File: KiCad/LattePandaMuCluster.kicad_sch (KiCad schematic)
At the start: 0 parts

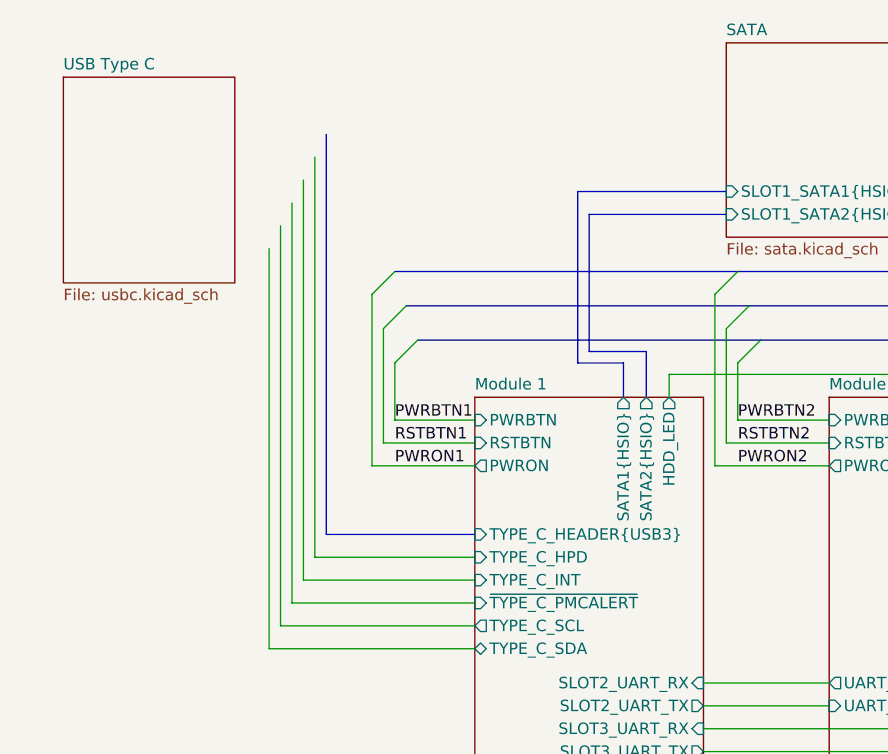
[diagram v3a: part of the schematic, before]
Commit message: Connect TPS65987D I2C and Interrupts
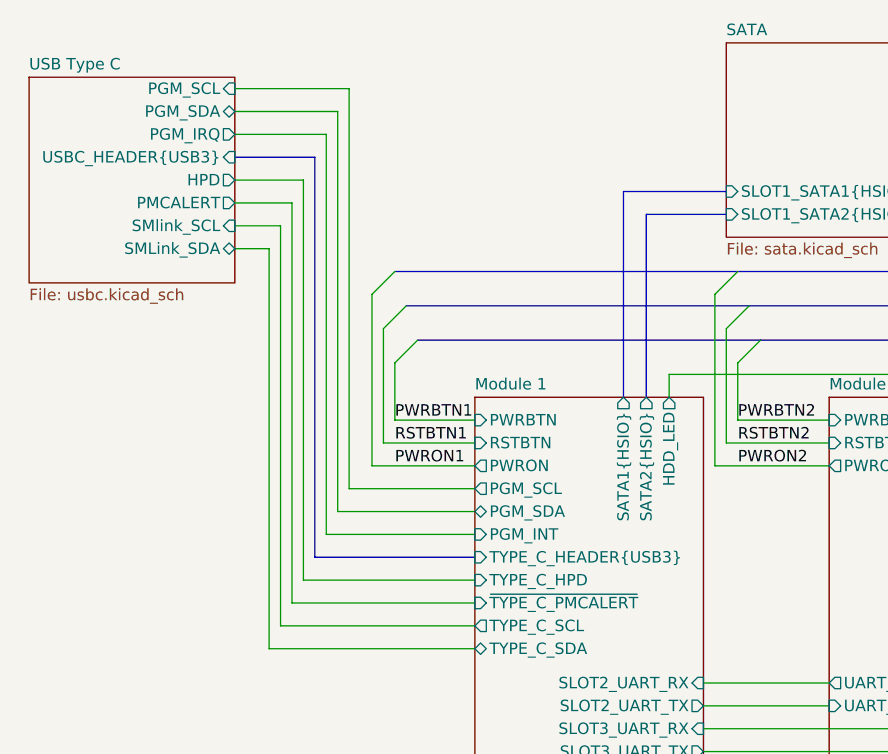
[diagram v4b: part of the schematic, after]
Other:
- sheet Module 1 ports: added PGM_INT, PGM_SCL, PGM_SDA; removed TYPE_C_INT
- sheet USB Type C ports: added HPD, PGM_IRQ, PGM_SCL, PGM_SDA, PMCALERT, SMLink_SDA, SMlink_SCL, USBC_HEADER{USB3}; removed none
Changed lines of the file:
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@@
 	(wire
 		(pts
-			(xy 81.28 158.75) (xy 81.28 168.91)
-		)
-		(stroke
-			(width 0)
-			(type default)
-		)
-	)
-	(bus
-		(pts
-			(xy 74.93 50.8) (xy 80.01 50.8)
+			(xy 46.99 69.85) (xy 63.5 69.85)
 		)
 		(stroke
@@
 		)
 	)
-	(bus
+	(wire
 		(pts
-			(xy 76.2 34.29) (xy 76.2 49.53)
+			(xy 81.28 158.75) (xy 81.28 168.91)
 		)
 		(stroke
@@
 	(wire
 		(pts
+			(xy 46.99 25.4) (xy 46.99 69.85)
+		)
+		(stroke
+			(width 0)
+			(type default)
+		)
+	)
+	(wire
+		(pts
 			(xy 88.9 101.6) (xy 196.85 101.6)
 		)
@@
 	(wire
 		(pts
-			(xy 45.72 72.39) (xy 45.72 27.94)
+			(xy 49.53 64.77) (xy 63.5 64.77)
+		)
+		(stroke
+			(width 0)
+			(type default)
+		)
+	)
+	(wire
+		(pts
+			(xy 44.45 74.93) (xy 44.45 30.48)
 		)
 		(stroke
@@
 		)
 	)
+	(wire
+		(pts
+			(xy 36.83 22.86) (xy 48.26 22.86)
+		)
+		(stroke
+			(width 0)
+			(type default)
+		)
+	)
 	(bus
 		(pts
@@
 	(wire
 		(pts
+			(xy 36.83 35.56) (xy 41.91 35.56)
+		)
+		(stroke
+			(width 0)
+			(type default)
+		)
+	)
+	(wire
+		(pts
 			(xy 43.18 77.47) (xy 43.18 33.02)
 		)
@@
 		)
 	)
+	(wire
+		(pts
+			(xy 36.83 38.1) (xy 40.64 38.1)
+		)
+		(stroke
+			(width 0)
+			(type default)
+		)
+	)
 	(bus
 		(pts
@@
 	(bus
 		(pts
-			(xy 76.2 49.53) (xy 82.55 49.53)
-		)
-		(stroke
-			(width 0)
-			(type default)
-		)
-	)
-	(bus
-		(pts
 			(xy 196.85 138.43) (xy 189.23 138.43)
 		)
@@
 	(bus
 		(pts
-			(xy 74.93 31.75) (xy 91.44 31.75)
+			(xy 80.01 31.75) (xy 91.44 31.75)
 		)
 		(stroke
@@
 	(bus
 		(pts
-			(xy 46.99 69.85) (xy 63.5 69.85)
+			(xy 45.72 72.39) (xy 63.5 72.39)
 		)
 		(stroke
@@
 	(bus
 		(pts
-			(xy 80.01 50.8) (xy 80.01 54.61)
-		)
-		(stroke
-			(width 0)
-			(type default)
-		)
-	)
-	(bus
-		(pts
 			(xy 218.44 153.67) (xy 220.98 153.67)
 		)
@@
 	(wire
 		(pts
+			(xy 36.83 20.32) (xy 49.53 20.32)
+		)
+		(stroke
+			(width 0)
+			(type default)
+		)
+	)
+	(wire
+		(pts
 			(xy 53.34 59.69) (xy 63.5 59.69)
 		)
@@
 	(wire
 		(pts
+			(xy 36.83 25.4) (xy 46.99 25.4)
+		)
+		(stroke
+			(width 0)
+			(type default)
+		)
+	)
+	(wire
+		(pts
 			(xy 90.17 162.56) (xy 90.17 168.91)
 		)
@@
 	(wire
 		(pts
+			(xy 49.53 20.32) (xy 49.53 64.77)
+		)
+		(stroke
+			(width 0)
+			(type default)
+		)
+	)
+	(wire
+		(pts
 			(xy 90.17 43.18) (xy 90.17 62.23)
 		)
@@
 	(wire
 		(pts
-			(xy 124.46 57.15) (xy 134.62 57.15)
+			(xy 36.83 33.02) (xy 43.18 33.02)
 		)
 		(stroke
@@
 		)
 	)
-	(bus
+	(wire
 		(pts
-			(xy 46.99 25.4) (xy 46.99 69.85)
+			(xy 124.46 57.15) (xy 134.62 57.15)
 		)
 		(stroke
@@
 	(bus
 		(pts
+			(xy 36.83 27.94) (xy 45.72 27.94)
+		)
+		(stroke
+			(width 0)
+			(type default)
+		)
+	)
+	(wire
+		(pts
+			(xy 48.26 22.86) (xy 48.26 67.31)
+		)
+		(stroke
+			(width 0)
+			(type default)
+		)
+	)
+	(bus
+		(pts
+			(xy 45.72 27.94) (xy 45.72 72.39)
+		)
+		(stroke
+			(width 0)
+			(type default)
+		)
+	)
+	(bus
+		(pts
 			(xy 128.27 154.94) (xy 76.2 154.94)
 		)
@@
 	(wire
 		(pts
-			(xy 44.45 74.93) (xy 44.45 30.48)
-		)
-		(stroke
-			(width 0)
-			(type default)
-		)
-	)
-	(wire
-		(pts
 			(xy 90.17 62.23) (xy 102.87 62.23)
 		)
@@
 	(bus
 		(pts
-			(xy 76.2 34.29) (xy 91.44 34.29)
+			(xy 82.55 34.29) (xy 91.44 34.29)
 		)
 		(stroke
@@
 	(bus
 		(pts
-			(xy 74.93 31.75) (xy 74.93 50.8)
+			(xy 80.01 31.75) (xy 80.01 54.61)
 		)
 		(stroke
@@
 	(wire
 		(pts
+			(xy 48.26 67.31) (xy 63.5 67.31)
+		)
+		(stroke
+			(width 0)
+			(type default)
+		)
+	)
+	(wire
+		(pts
 			(xy 123.19 46.99) (xy 123.19 59.69)
 		)
@@
 	(wire
 		(pts
-			(xy 63.5 74.93) (xy 44.45 74.93)
+			(xy 36.83 30.48) (xy 44.45 30.48)
 		)
 		(stroke
@@
 	(bus
 		(pts
-			(xy 82.55 49.53) (xy 82.55 54.61)
+			(xy 82.55 34.29) (xy 82.55 54.61)
 		)
 		(stroke
@@
 	(wire
 		(pts
-			(xy 63.5 72.39) (xy 45.72 72.39)
+			(xy 63.5 74.93) (xy 44.45 74.93)
 		)
 		(stroke
@@
 		)
 		(pin "TYPE_C_HEADER{USB3}" input
-			(at 63.5 69.85 180)
+			(at 63.5 72.39 180)
 			(effects
 				(font
@@
 		)
 		(pin "TYPE_C_HPD" input
-			(at 63.5 72.39 180)
-			(effects
-				(font
-					(size 1.27 1.27)
-				)
-				(justify left)
-			)
-		)
-		(pin "TYPE_C_INT" input
 			(at 63.5 74.93 180)
 			(effects
@@
 			)
 		)
+		(pin "PGM_INT" input
+			(at 63.5 69.85 180)
+			(effects
+				(font
+					(size 1.27 1.27)
+				)
+				(justify left)
+			)
+		)
+		(pin "PGM_SCL" output
+			(at 63.5 64.77 180)
+			(effects
+				(font
+					(size 1.27 1.27)
+				)
+				(justify left)
+			)
+		)
+		(pin "PGM_SDA" bidirectional
+			(at 63.5 67.31 180)
+			(effects
+				(font
+					(size 1.27 1.27)
+				)
+				(justify left)
+			)
+		)
 		(instances
 			(project "LattePandaMuCluster"
@@
 	)
 	(sheet
-		(at 17.78 19.05)
-		(size 19.05 22.86)
+		(at 13.97 19.05)
+		(size 22.86 22.86)
 		(exclude_from_sim no)
 		(in_bom yes)
@@
 		)
 		(property "Sheetname" "USB Type C"
-			(at 17.78 18.3384 0)
+			(at 13.97 18.3384 0)
 			(effects
 				(font
@@
 		)
 		(property "Sheetfile" "usbc.kicad_sch"
-			(at 17.78 42.4946 0)
+			(at 13.97 42.4946 0)
 			(effects
 				(font
@@
 			)
 		)
+		(pin "HPD" output
+			(at 36.83 30.48 0)
+			(effects
+				(font
+					(size 1.27 1.27)
+				)
+				(justify right)
+			)
+		)
+		(pin "PGM_IRQ" output
+			(at 36.83 25.4 0)
+			(effects
+				(font
+					(size 1.27 1.27)
+				)
+				(justify right)
+			)
+		)
+		(pin "PGM_SCL" input
+			(at 36.83 20.32 0)
+			(effects
+				(font
+					(size 1.27 1.27)
+				)
+				(justify right)
+			)
+		)
+		(pin "PGM_SDA" bidirectional
+			(at 36.83 22.86 0)
+			(effects
+				(font
+					(size 1.27 1.27)
+				)
+				(justify right)
+			)
+		)
+		(pin "PMCALERT" output
+			(at 36.83 33.02 0)
+			(effects
+				(font
+					(size 1.27 1.27)
+				)
+				(justify right)
+			)
+		)
+		(pin "SMlink_SCL" input
+			(at 36.83 35.56 0)
+			(effects
+				(font
+					(size 1.27 1.27)
+				)
+				(justify right)
+			)
+		)
+		(pin "SMLink_SDA" bidirectional
+			(at 36.83 38.1 0)
+			(effects
+				(font
+					(size 1.27 1.27)
+				)
+				(justify right)
+			)
+		)
+		(pin "USBC_HEADER{USB3}" input
+			(at 36.83 27.94 0)
+			(effects
+				(font
+					(size 1.27 1.27)
+				)
+				(justify right)
+			)
+		)

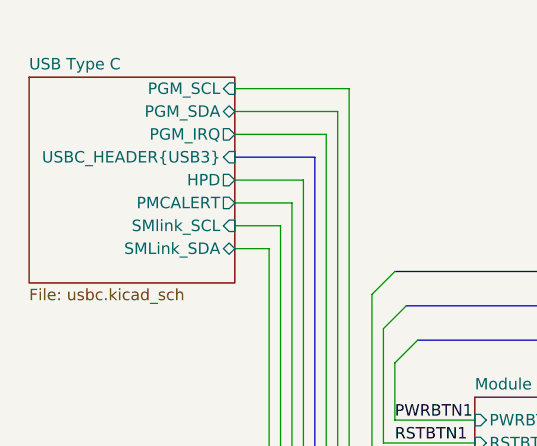
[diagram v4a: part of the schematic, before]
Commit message: Finish wiring TPS65987D
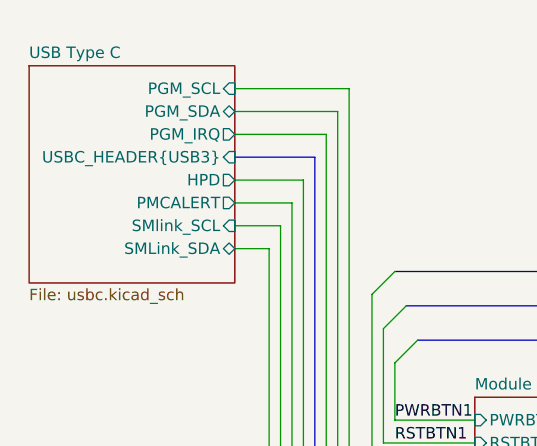
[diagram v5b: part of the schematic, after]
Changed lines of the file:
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@@
 	)
 	(sheet
-		(at 13.97 19.05)
-		(size 22.86 22.86)
+		(at 13.97 17.78)
+		(size 22.86 24.13)
 		(exclude_from_sim no)
 		(in_bom yes)
@@
 		)
 		(property "Sheetname" "USB Type C"
-			(at 13.97 18.3384 0)
+			(at 13.97 17.0684 0)
 			(effects
 				(font

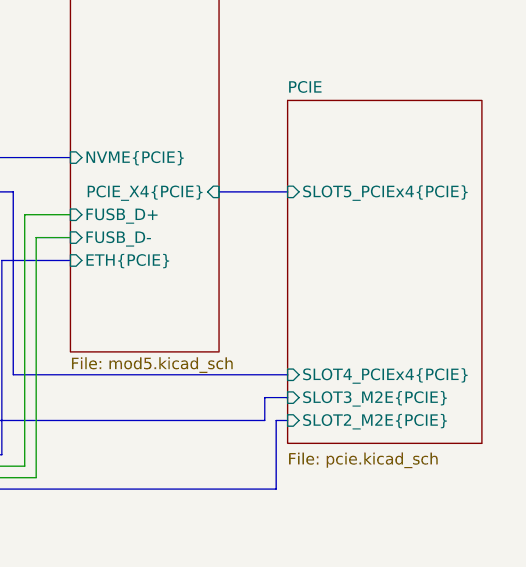
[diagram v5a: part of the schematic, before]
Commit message: Remove 0.95V Power Supply, Replace 3.3V Standby Power Supply
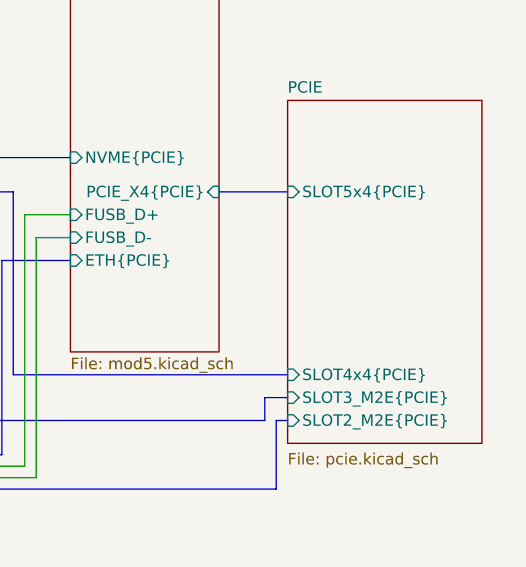
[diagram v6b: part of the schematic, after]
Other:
- sheet PCIE ports: added SLOT4x4{PCIE}, SLOT5x4{PCIE}; removed SLOT4_PCIEx4{PCIE}, SLOT5_PCIEx4{PCIE}
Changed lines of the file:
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@@
 			)
 		)
-		(pin "SLOT4_PCIEx4{PCIE}" input
+		(pin "SLOT4x4{PCIE}" input
 			(at 220.98 151.13 180)
 			(effects
@@
 			)
 		)
-		(pin "SLOT5_PCIEx4{PCIE}" input
+		(pin "SLOT5x4{PCIE}" input
 			(at 220.98 130.81 180)
 			(effects

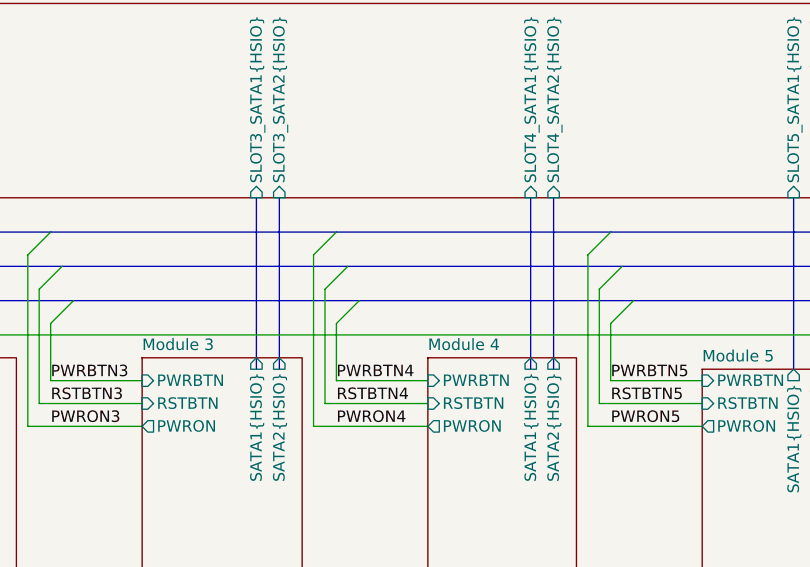
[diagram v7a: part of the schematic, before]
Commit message: Fix esd diodes, add some footprints.
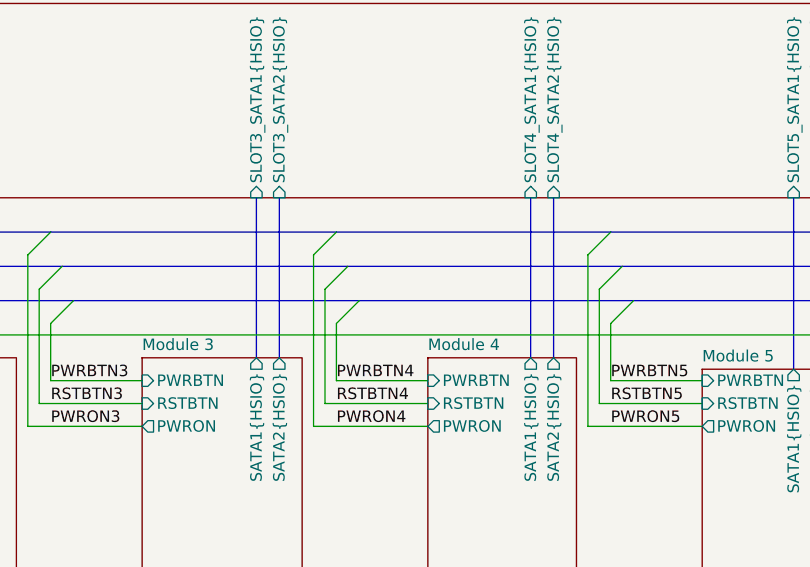
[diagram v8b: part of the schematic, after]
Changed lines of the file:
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@@
 	(bus
 		(pts
-			(xy 180.34 36.83) (xy 180.34 55.88)
+			(xy 180.34 36.83) (xy 180.34 54.61)
 		)
 		(stroke
@@
 	(bus
 		(pts
-			(xy 149.86 36.83) (xy 149.86 55.88)
+			(xy 149.86 36.83) (xy 149.86 54.61)
 		)
 		(stroke
@@
 	(bus
 		(pts
-			(xy 147.32 36.83) (xy 147.32 55.88)
+			(xy 147.32 36.83) (xy 147.32 54.61)
 		)
 		(stroke
@@
 	(bus
 		(pts
-			(xy 177.8 36.83) (xy 177.8 55.88)
-		)
-		(stroke
+			(xy 177.8 36.83) (xy 177.8 54.61)
+		)
+		(stroke
